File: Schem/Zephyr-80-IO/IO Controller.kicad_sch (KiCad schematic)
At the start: 31 parts, among them IC1 Z80CTC, IC2 Z80SIO, IC3 Z80SIO, J5 Conn_01x08_Pin, SW1 SW_Push, SW2 SW_Push, U15 PIC18F57Q84-I/PT, U2 74AHC1G125, U3 74AHC1G125, U4 74AHC595, U5 74AHC595, U6 74HC138

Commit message: Added all the manufacturer part numbers to the KiCad schematics and PCB files. This will make it easier to order the parts for the project and ensure that the correct components are used. I also removed some of the old schematics that were no longer needed, such as the BaudClock, ConsolePort, DeviceSelectDecode, GPIOUserSerial, IO Controller, UserPorts, Video, and Z80HomeBrew schematics. These changes will help to streamline the design and make it easier to understand.
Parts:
- J5: now left out of the parts list
- SW1, SW2: MANUFACTURER_PART_NUMBER (none) -> CRCW06034K70FKEA
- U15: MANUFACTURER_PART_NUMBER (none) -> PIC18F57Q84-I/PT
- U2, U3: MANUFACTURER_PART_NUMBER (none) -> SN74AHC1G125DCKR
- U4, U5: MANUFACTURER_PART_NUMBER (none) -> 74AHC595PW,118
- U6: MANUFACTURER_PART_NUMBER (none) -> SN74HC138PWR
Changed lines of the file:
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@@
 			)
 		)
+		(property "MANUFACTURER_PART_NUMBER" "SN74AHC1G125DCKR"
+			(at 227.33 177.8 0)
+			(effects
+				(font
+					(size 1.27 1.27)
+				)
+				(hide yes)
+			)
+		)
 		(pin "1"
 		)
@@
 			)
 		)
+		(property "MANUFACTURER_PART_NUMBER" "CRCW06034K70FKEA"
+			(at 62.23 118.11 0)
+			(effects
+				(font
+					(size 1.27 1.27)
+				)
+				(hide yes)
+			)
+		)
 		(pin "2"
 		)
@@
 			)
 		)
+		(property "MANUFACTURER_PART_NUMBER" "PIC18F57Q84-I/PT"
+			(at 120.65 80.01 0)
+			(effects
+				(font
+					(size 1.27 1.27)
+				)
+				(hide yes)
+			)
+		)
 		(pin "9"
 		)
@@
 			)
 		)
+		(property "MANUFACTURER_PART_NUMBER" "SN74HC138PWR"
+			(at 218.44 364.49 0)
+			(effects
+				(font
+					(size 1.27 1.27)
+				)
+				(hide yes)
+			)
+		)
 		(pin "7"
 		)
@@
 			)
 		)
+		(property "MANUFACTURER_PART_NUMBER" "CRCW06034K70FKEA"
+			(at 62.23 177.8 0)
+			(effects
+				(font
+					(size 1.27 1.27)
+				)
+				(hide yes)
+			)
+		)
 		(pin "1"
 		)
@@
 			)
 		)
+		(property "MANUFACTURER_PART_NUMBER" "74AHC595PW,118"
+			(at 273.05 288.29 0)
+			(effects
+				(font
+					(size 1.27 1.27)
+				)
+				(hide yes)
+			)
+		)
 		(pin "6"
 		)
@@
 			)
 		)
+		(property "MANUFACTURER_PART_NUMBER" "74AHC595PW,118"
+			(at 208.28 288.29 0)
+			(effects
+				(font
+					(size 1.27 1.27)
+				)
+				(hide yes)
+			)
+		)
 		(pin "6"
 		)
@@
 			)
 		)
+		(property "MANUFACTURER_PART_NUMBER" "SN74AHC1G125DCKR"
+			(at 223.52 208.28 0)
+			(effects
+				(font
+					(size 1.27 1.27)
+				)
+				(hide yes)
+			)
+		)
 		(pin "2"
 		)
@@
 		(unit 1)
 		(exclude_from_sim no)
-		(in_bom yes)
+		(in_bom no)
 		(on_board yes)
 		(dnp no)

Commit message: Fixed manufacturer part number
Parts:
- SW1, SW2: MANUFACTURER_PART_NUMBER CRCW06034K70FKEA -> (none)
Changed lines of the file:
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@@
 			)
 		)
-		(property "MANUFACTURER_PART_NUMBER" "CRCW06034K70FKEA"
+		(property "MANUFACTURER_PART_NUMBER" ""
 			(at 62.23 118.11 0)
 			(effects
@@
 			)
 		)
-		(property "MANUFACTURER_PART_NUMBER" "CRCW06034K70FKEA"
+		(property "MANUFACTURER_PART_NUMBER" ""
 			(at 62.23 177.8 0)
 			(effects

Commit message: Fixed io controller 1.27mm pitch header to 2.54mm pitch header.
First battle scars :)
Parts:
- D1, SW1, SW2: footprint Connector_PinHeader_1.27mm:PinHeader_1x02_P1.27mm_Vertical -> Connector_PinHeader_2.54mm:PinHeader_1x02_P2.54mm_Vertical
- J5: footprint Connector_PinHeader_1.27mm:PinHeader_1x08_P1.27mm_Vertical -> Connector_PinHeader_2.54mm:PinHeader_1x08_P2.54mm_Vertical
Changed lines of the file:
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@@
 			)
 		)
-		(property "Footprint" "Connector_PinHeader_1.27mm:PinHeader_1x02_P1.27mm_Vertical"
+		(property "Footprint" "Connector_PinHeader_2.54mm:PinHeader_1x02_P2.54mm_Vertical"
 			(at 62.23 113.03 0)
 			(effects
@@
 			)
 		)
-		(property "Footprint" "Connector_PinHeader_1.27mm:PinHeader_1x02_P1.27mm_Vertical"
+		(property "Footprint" "Connector_PinHeader_2.54mm:PinHeader_1x02_P2.54mm_Vertical"
 			(at 62.23 146.05 0)
 			(effects
@@
 			)
 		)
-		(property "Footprint" "Connector_PinHeader_1.27mm:PinHeader_1x02_P1.27mm_Vertical"
+		(property "Footprint" "Connector_PinHeader_2.54mm:PinHeader_1x02_P2.54mm_Vertical"
 			(at 62.23 172.72 0)
 			(effects
@@
 			)
 		)
-		(property "Footprint" "Connector_PinHeader_1.27mm:PinHeader_1x08_P1.27mm_Vertical"
+		(property "Footprint" "Connector_PinHeader_2.54mm:PinHeader_1x08_P2.54mm_Vertical"
 			(at 90.17 118.11 0)
 			(effects

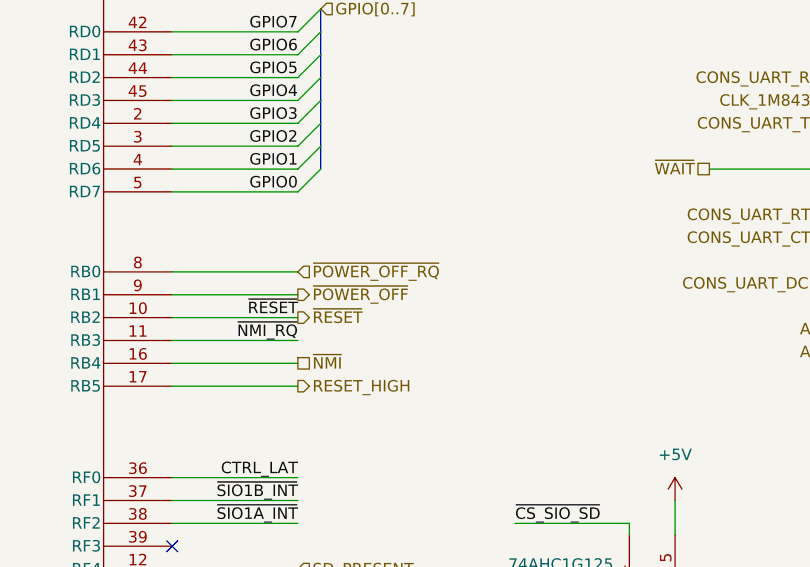
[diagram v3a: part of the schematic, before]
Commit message: Implemented IO Controller side of power management protocol and fixed the naming in the diagrams
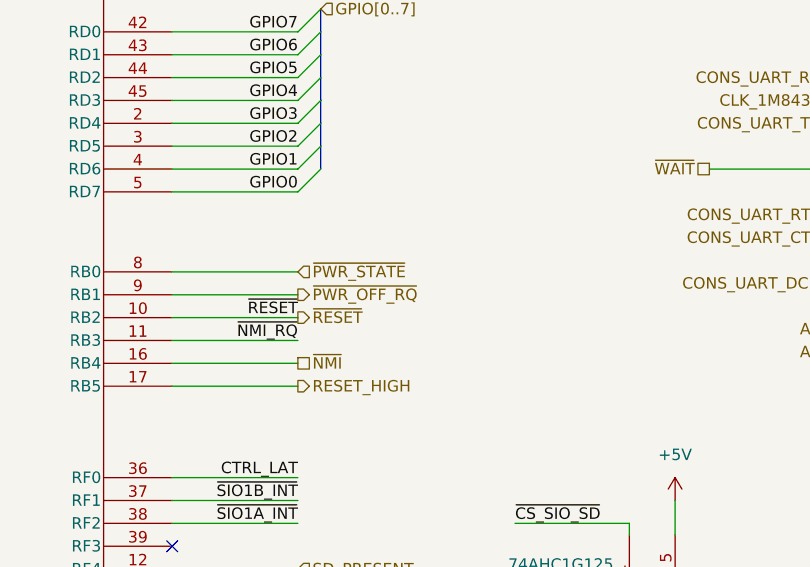
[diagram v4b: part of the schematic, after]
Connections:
- net ~{POWER_OFF_RQ} renamed ~{PWR_STATE}
- net ~{POWER_OFF} renamed ~{PWR_OFF_RQ}

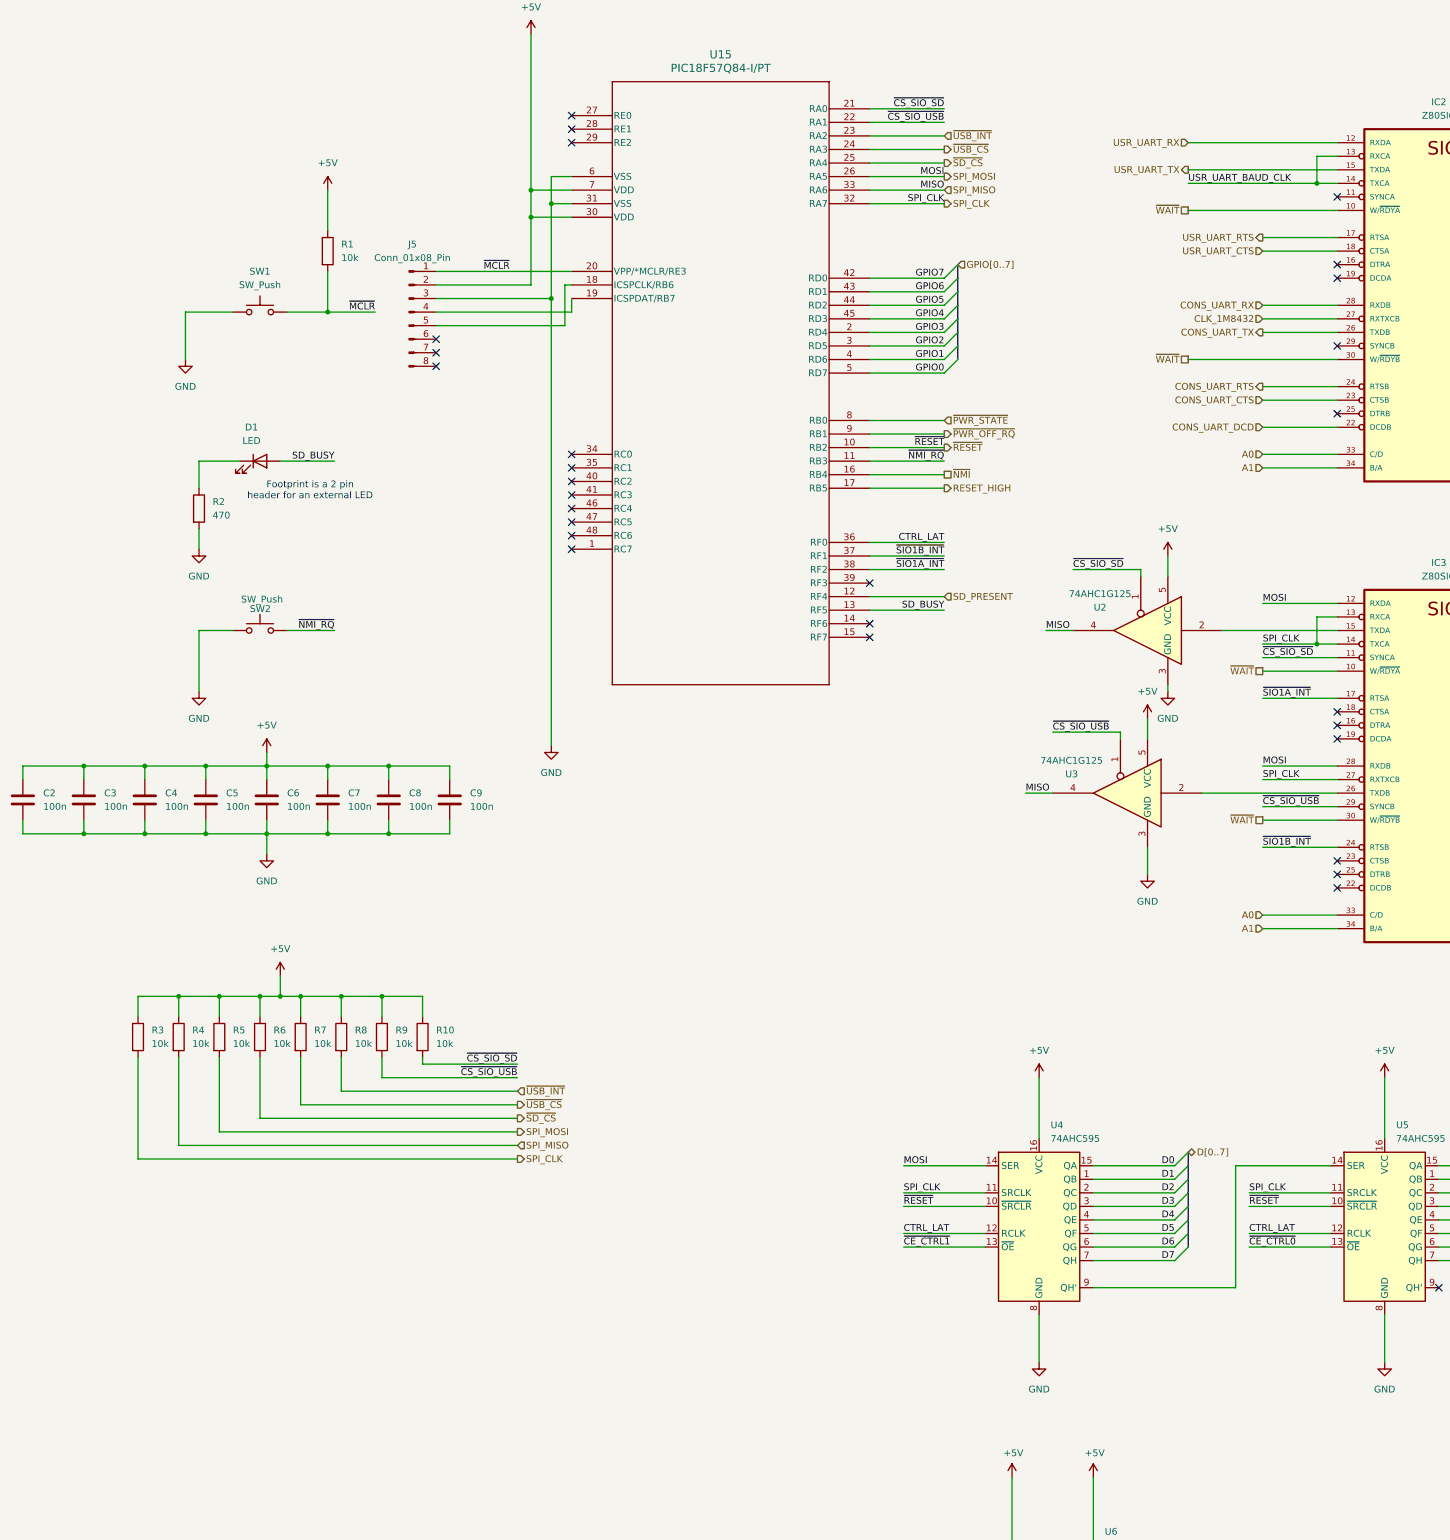
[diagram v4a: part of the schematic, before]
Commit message: Updated the IO Controller to properly support SDLC and SPI.
* Separated SPI1 and SPI2 and associated to the right pins.
      SPI1 is for devices (USB, SD Card and Controllers)
      SPI2 is for the SDLC controller (Z80 SIO1/A and B)

* Fixed the 1.27mm vs 2.54mm pin headers
* Fixed the power sequencing
* Fixed the pull ups
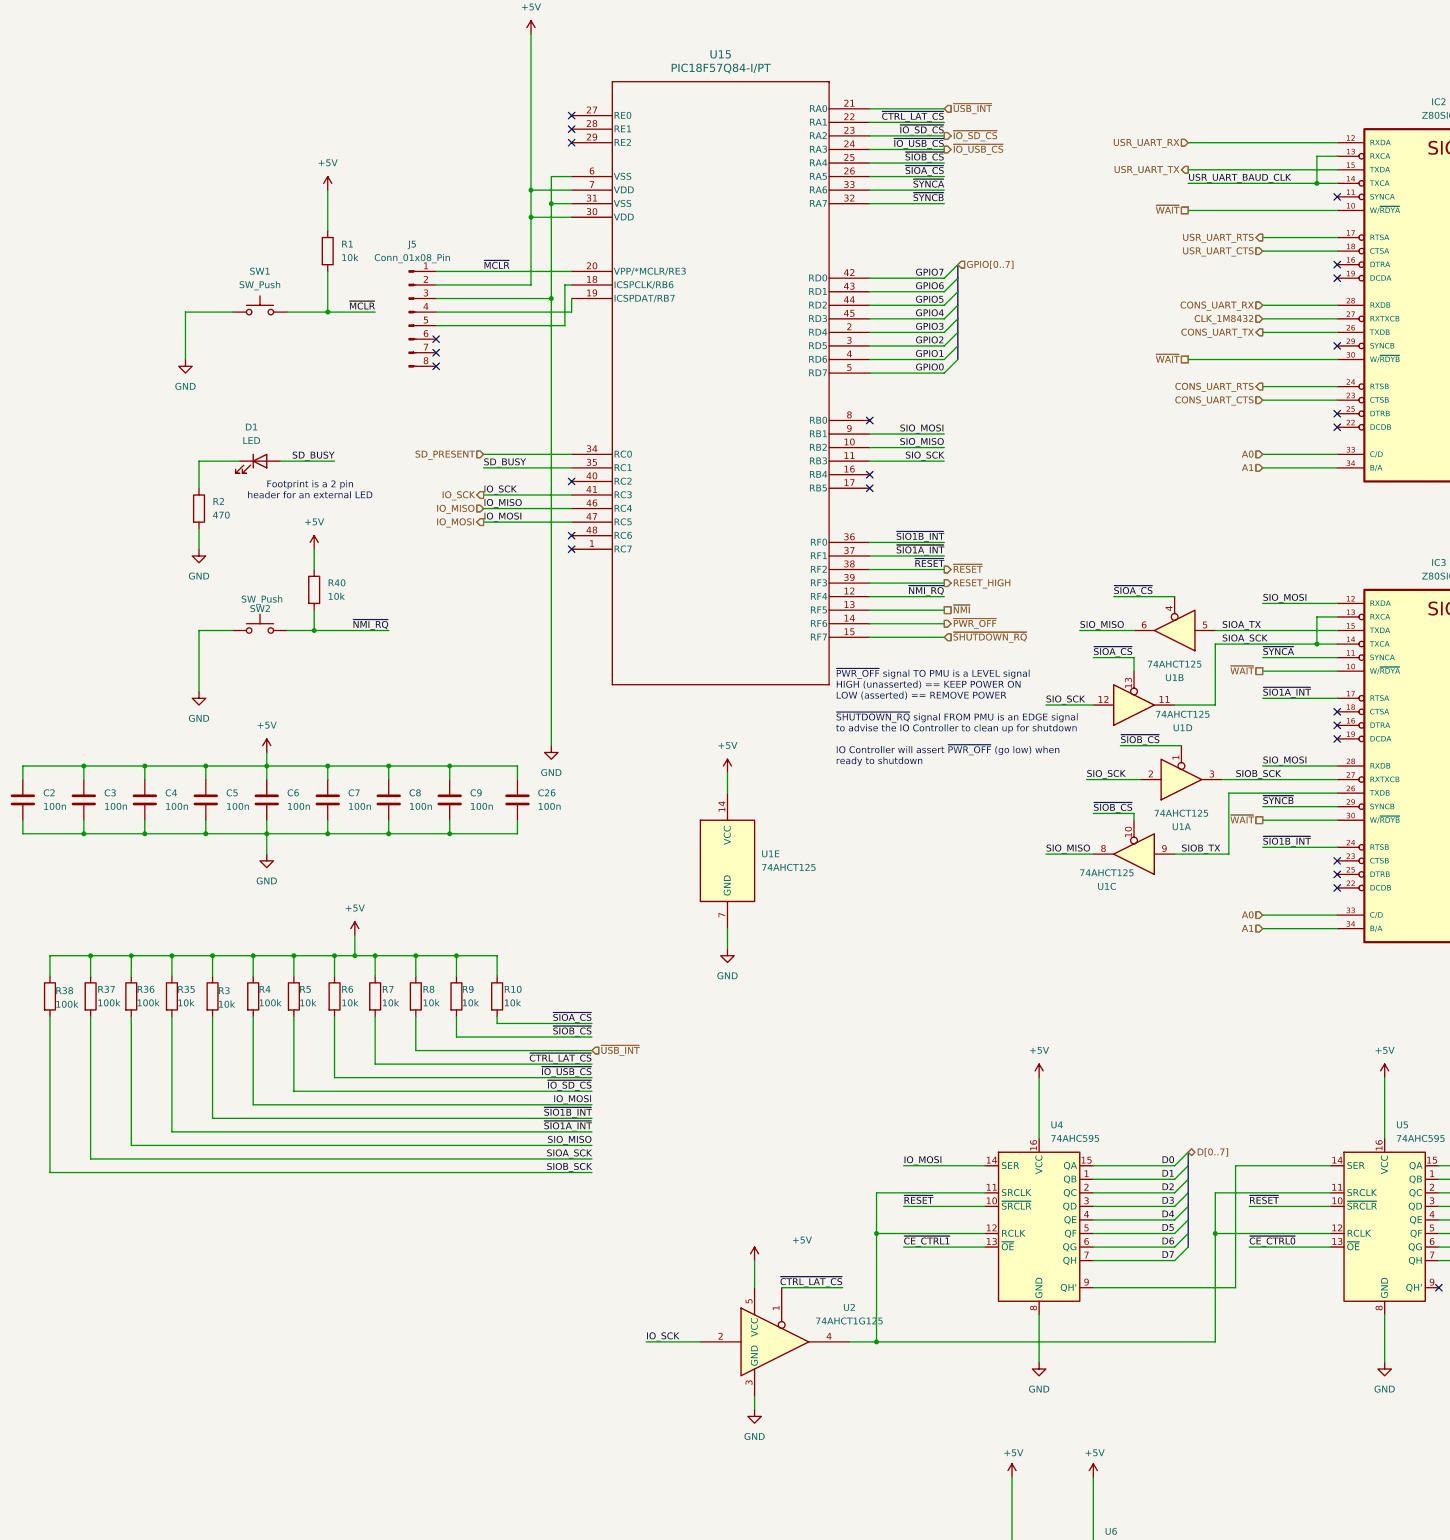
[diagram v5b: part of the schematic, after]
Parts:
- removed U2, U3: 74AHC1G125, Package_TO_SOT_SMD:SC-74A-5_1.55x2.9mm_P0.95mm, symbol 74xGxx:74AHC1G125
- added C26: 100n, Capacitor_SMD:C_0603_1608Metric, symbol Device:C
- added R35, R40: 10k, Resistor_SMD:R_0603_1608Metric, symbol Device:R
- added R36, R37, R38: 100k, Resistor_SMD:R_0603_1608Metric, symbol Device:R
- added U1: 74AHCT125, Package_SO:TSSOP-14_4.4x5mm_P0.65mm, symbol 74xx:74AHCT125
- added U2: 74AHCT1G125, Package_TO_SOT_SMD:SOT-23-5, symbol 74xGxx:74AHCT1G125
- R4: value 10k -> 100k
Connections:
- net +5V: now also C26.1, R35.1, R36.1, R37.1, R38.1, R40.1, U1.14 (VCC), U2.5 (VCC)
- net GND: now also C26.2, U1.7 (GND), U2.3 (GND)
- net RESET_HIGH: now also U15.39 (RF3); no longer U15.17 (RB5)
- net SD_BUSY: now also U15.35 (RC1); no longer U15.13 (RF5)
- net SD_PRESENT: now also U15.34 (RC0); no longer U15.12 (RF4)
- net ~{NMI_RQ}: now also U15.12 (RF4), R40.2; no longer U15.11 (RB3)
- net ~{NMI}: now also U15.13 (RF5); no longer U15.16 (RB4)
- net ~{RESET}: now also U15.38 (RF2); no longer U15.10 (RB2)
- net ~{SIO1A_INT}: now also U15.37 (RF1), R35.2; no longer U15.38 (RF2)
- net ~{SIO1B_INT}: now also R3.2, U15.36 (RF0); no longer U15.37 (RF1)
- net ~{USB_INT}: now also U15.21 (RA0); no longer U15.23 (RA2)
- net SIOA_TX: now reaches IC3.15 (TXDA)
- net SIOA_TX: now also U1.5
- net SIOB_TX: now reaches IC3.26 (TXDB)
- net SIOB_TX: now also U1.9
- net ~{PWR_OFF}: now reaches U15.14 (RF6)
- net ~{SHUTDOWN_RQ}: now reaches U15.15 (RF7)
- net IO_SCK: now reaches U15.41 (RC3)
- net IO_SCK: now also U2.2
- net IO_MISO: now reaches U15.46 (RC4)
- net IO_MOSI: now reaches U15.47 (RC5)
- net IO_MOSI: now also R4.2, U4.14 (SER)
- net CONS_UART_DCD: no longer names the net of IC2.22 (DCDB)
- net CTRL_LAT: no longer names the net of U4.12 (RCLK), U5.12 (RCLK)
- net CTRL_LAT: now also U4.11 (SRCLK), U5.11 (SRCLK), U2.4; no longer U15.36 (RF0)
- removed net SPI_CLK: IC3.13 (RXCA), IC3.14 (TXCA), IC3.27 (RXTXCB), R3.2, U15.32 (RA7), U4.11 (SRCLK), U5.11 (SRCLK)
- net SPI_MISO renamed ~{SYNCA}
- net ~{SYNCA}: now also IC3.11 (SYNCA); no longer R4.2
- removed net SPI_MOSI: IC3.12 (RXDA), IC3.28 (RXDB), R5.2, U15.26 (RA5), U4.14 (SER)
- removed net ~{CS_SIO_SD}: IC3.11 (SYNCA), R10.2, U15.21 (RA0)
- removed net ~{CS_SIO_USB}: IC3.29 (SYNCB), R9.2, U15.22 (RA1)
- net ~{PWR_OFF_RQ} renamed SIO_MOSI
- net SIO_MOSI: now also IC3.12 (RXDA), IC3.28 (RXDB)
- net ~{PWR_STATE}: no longer names the net of U15.8 (RB0)
- net ~{SD_CS} renamed ~{IO_USB_CS}
- net ~{IO_USB_CS}: now also U15.24 (RA3); no longer U15.25 (RA4)
- net ~{USB_CS} renamed ~{CTRL_LAT_CS}
- net ~{CTRL_LAT_CS}: now also U15.22 (RA1), U2.1; no longer U15.24 (RA3)
- new net SIOA_SCK: IC3.13 (RXCA), IC3.14 (TXCA), R37.2, U1.11
- new net SIOB_SCK: IC3.27 (RXTXCB), R38.2, U1.3
- new net SIO_MISO: R36.2, U1.6, U1.8, U15.10 (RB2)
- new net SIO_SCK: U1.12, U1.2, U15.11 (RB3)
- new net ~{IO_SD_CS}: R5.2, U15.23 (RA2)
- new net ~{SIOA_CS}: R10.2, U1.13, U1.4, U15.26 (RA5)
- new net ~{SIOB_CS}: R9.2, U1.1, U1.10, U15.25 (RA4)
- new net ~{SYNCB}: IC3.29 (SYNCB), U15.32 (RA7)
- no-connect marks 35 -> 31
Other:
- note added: "~{PWR_OFF} signal TO PMU is a LEVEL signal HIGH (unasserted) == KEEP POWER ON LOW (asserted) == REMOVE POWER ~{SHUTDOWN_RQ} signal FROM PMU is an EDGE signal to advise the IO Controller to clean up for shutdown IO Controller will assert ~{PWR_OFF} (go low) when ready to shutdown"
- moved on the sheet: R10, R3, R4, R5, R6, R7, R8, R9

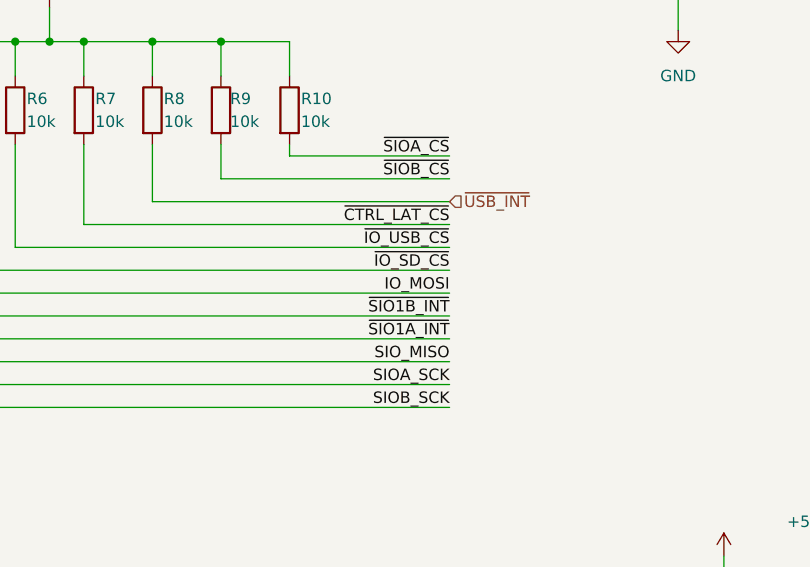
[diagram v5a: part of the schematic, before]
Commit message: Removed the rotary switch selector
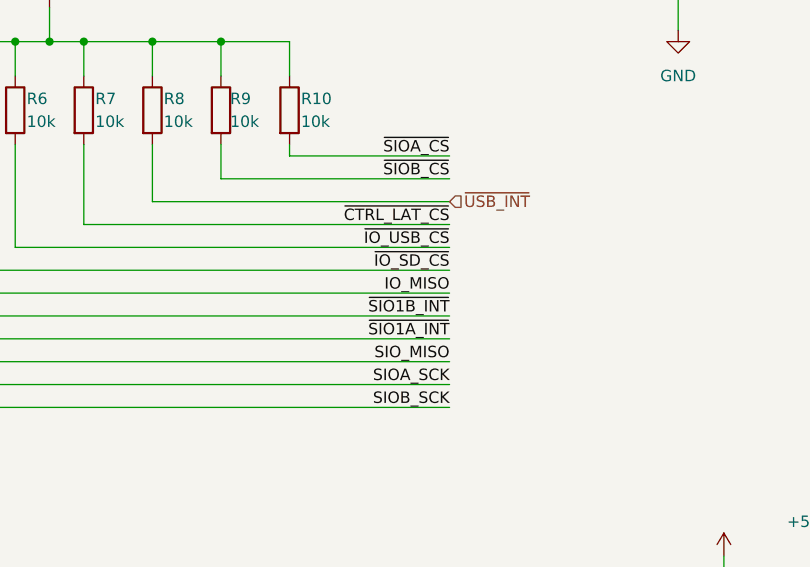
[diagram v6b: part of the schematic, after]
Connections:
- net IO_MISO: now also R4.2
- net IO_MOSI: no longer R4.2
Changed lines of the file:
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@@
 		)
 	)
-	(label "IO_MOSI"
+	(label "IO_MISO"
 		(at 124.46 266.7 180)
 		(effects
